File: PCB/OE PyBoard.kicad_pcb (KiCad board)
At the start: 4 copper layers, 33 x 41.9 mm, 57 parts, among them J3 USB4105-GF-A, J4 Conn_02x03_Odd_Even, J6 Conn_01x08, J7 Conn_01x08, U2 STM32F405RGT6, U3 MCP1700T, X2 12 MHz, X3 32.768 kHz

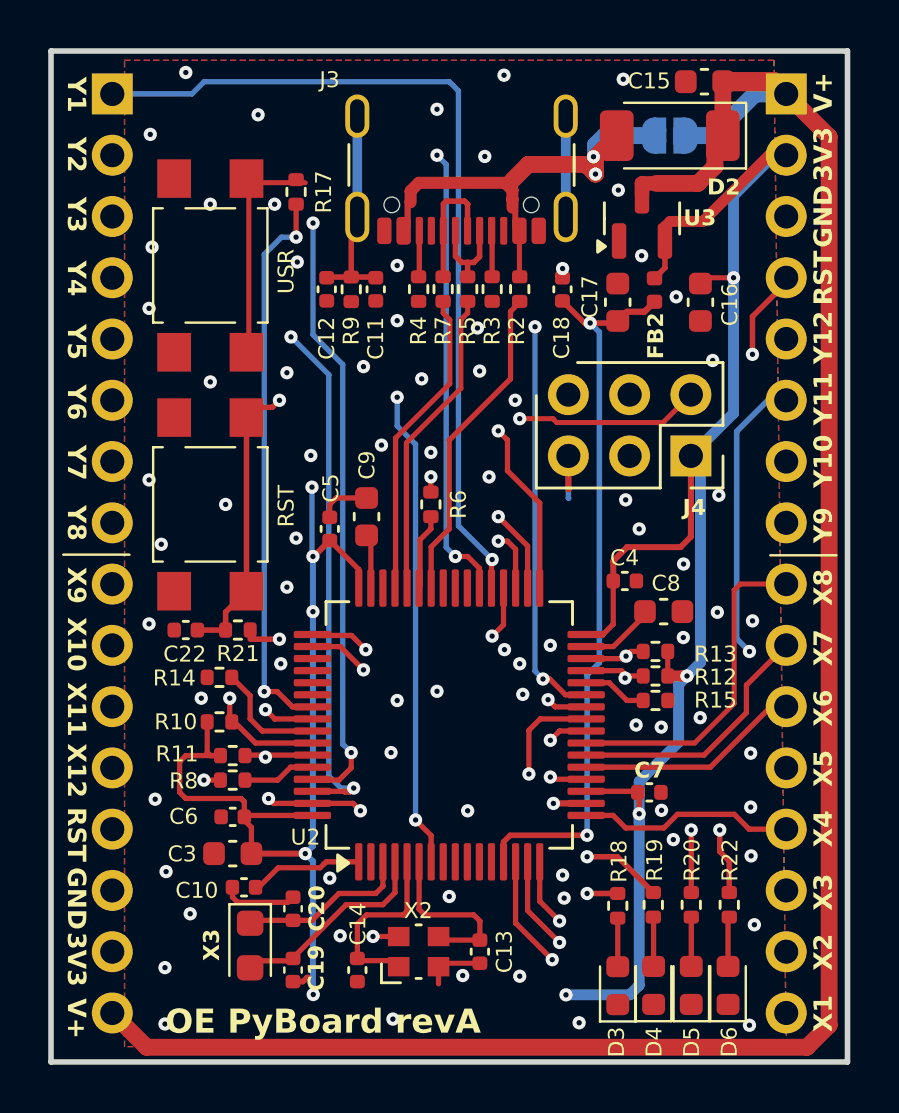
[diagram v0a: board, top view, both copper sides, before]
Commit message: . preparada para produção
- demoninação rev.B passada a rev.A
- criados ficheiros de produção:
  . Gerbers & Drills
  . IPC-2581
  . OE PyBoard BOM
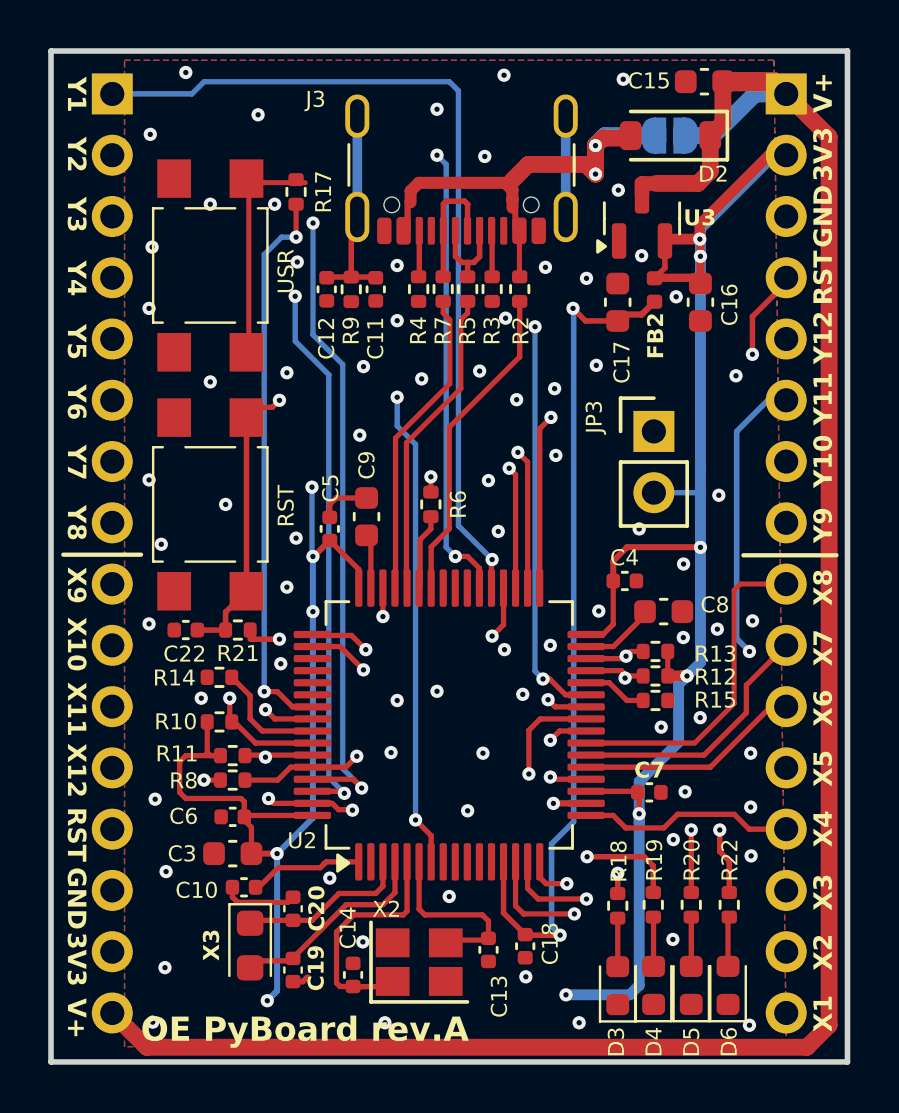
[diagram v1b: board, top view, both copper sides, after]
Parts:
- removed J4: Conn_02x03_Odd_Even, Connector_PinSocket_2.54mm:PinSocket_2x03_P2.54mm_Vertical
- added JP3: Jumper, Connector_PinHeader_2.54mm:PinHeader_1x02_P2.54mm_Vertical, F.Cu at (150.5, 110.0)
- D2: footprint Diode_SMD:D_SOD-128 -> Diode_SMD:D_SOD-123
- X2: footprint Crystal:Crystal_SMD_Abracon_ABM10-4Pin_2.5x2.0mm -> Crystal:Crystal_SMD_Abracon_ABM8AIG-4Pin_3.2x2.5mm
- moved C18 27.3 mm to (145.1, 131.3), turned to -90 degrees
- moved X2 0.43 mm to (140.7, 132.0), turned to 0 degrees
- moved C13 0.36 mm to (143.6, 131.5)
- moved C14 0.27 mm to (138.0, 132.5), turned to 90 degrees
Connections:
- net /PA14-JTCK renamed /PA14-GRN
- net /PA15-JTDI renamed /PA15-YEL
- net /PB4-NJTRST renamed /PB4-BLU
- R18 pad 1: /PB6-JTDO -> /PA13-RED
- U2 pad 46: /PA13-TMS -> /PA13-RED
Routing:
- net /BOOT0: track 3.01 -> 30.9 mm, vias 0 -> 2
- net /PB6-JTDO: track 23.2 -> 0.00 mm, vias 1 -> 0
- net /PA13-RED: track 0.00 -> 22.4 mm, vias 0 -> 3
- net /PA14-GRN: track 40.6 -> 23.8 mm, vias 4 -> 3
- net /PB4-BLU: track 40.4 -> 28.2 mm, vias 4 -> 3
- net /PA15-YEL: track 39.4 -> 27.7 mm, vias 4 -> 3
- net GND: track 19.9 -> 11.8 mm, vias 75 -> 72
- net /VDDA: track 30.5 -> 35.4 mm
- net /N3: track 7.12 -> 10.8 mm
- net /PB13-Y6: track 21.5 -> 23.5 mm
- net /PB12-Y5: track 24.8 -> 26.8 mm
- net /PB14-Y7: track 19.8 -> 21.6 mm
- net /PB8-Y3: track 33.1 -> 34.5 mm
- net +3V3: track 134.5 -> 135.9 mm, vias 11 -> 13
- net /PA2-X3: track 12.7 -> 11.5 mm
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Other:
- board text added: "OE PyBoard rev.A"
- board text removed: "OE PyBoard revA"
